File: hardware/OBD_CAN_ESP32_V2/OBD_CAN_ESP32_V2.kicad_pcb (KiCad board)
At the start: 2 copper layers, 64 x 36 mm, 39 parts, among them J1 OBD-II INPUT, J3 ESP32_S3_DEVKITC_J1, J4 ESP32_S3_DEVKITC_J3, Q1 Q_PMOS_GDS, U1 SN65HVD230, U2 TPS54360BDDA

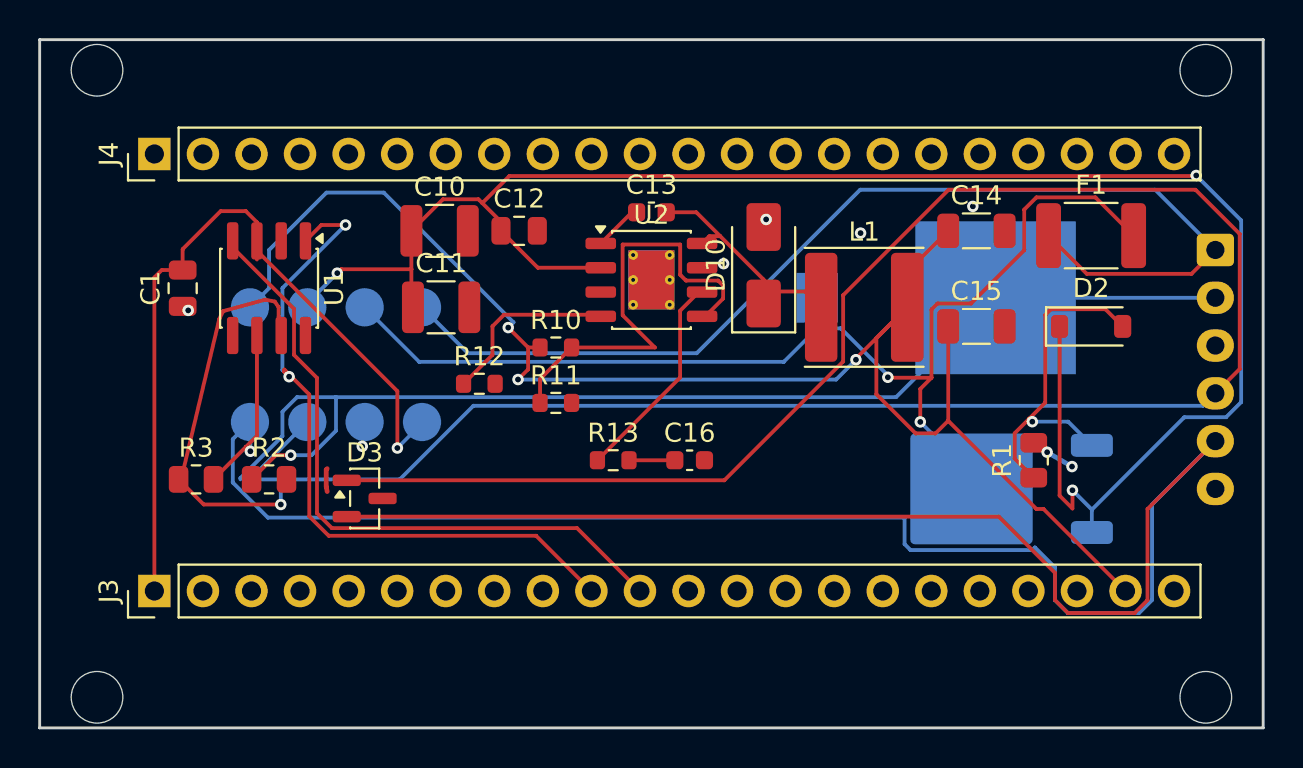
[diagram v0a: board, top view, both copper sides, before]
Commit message: V2 PCB 경고 정리: refdes를 Fab 레이어로, J1 실크 클리핑, 죽은 배선 제거, D1 풋프린트 정규화 + 조립도면 추가
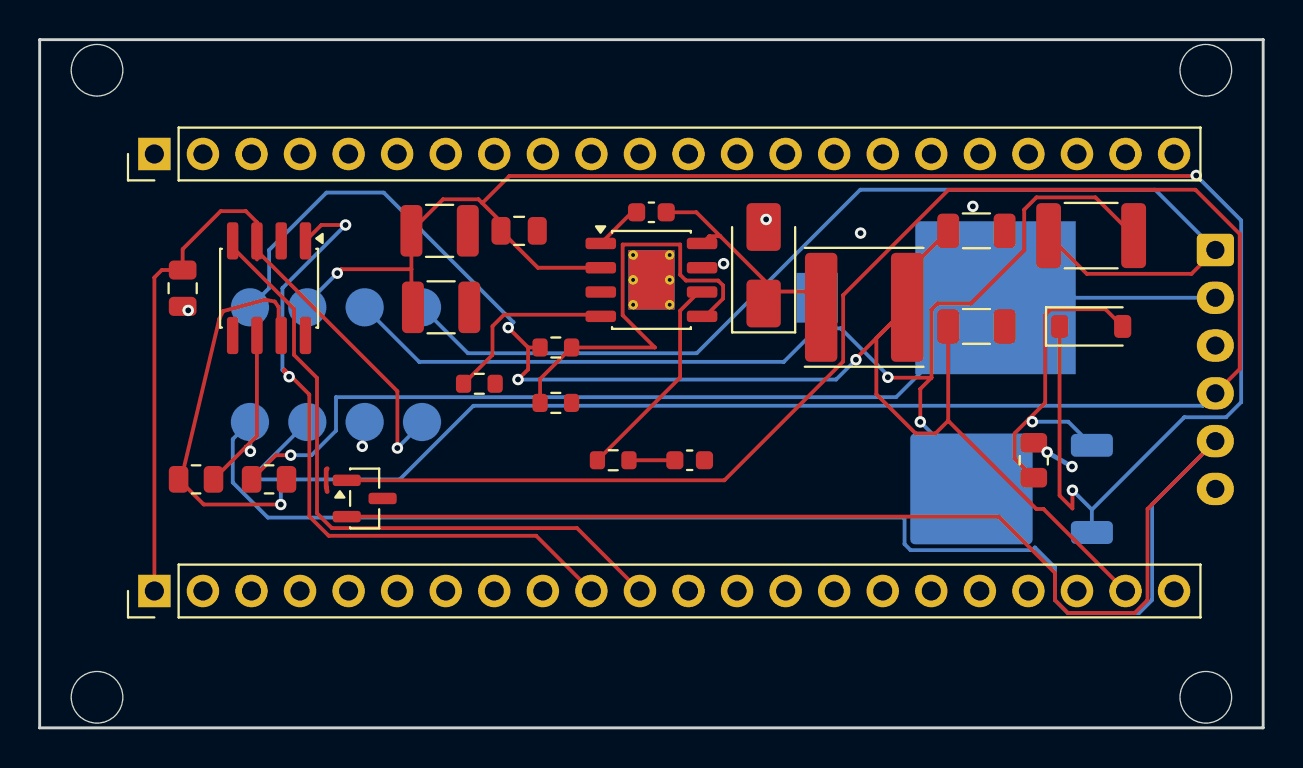
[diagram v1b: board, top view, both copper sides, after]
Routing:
- net /CHASSIS_GND: track 62.9 -> 55.4 mm
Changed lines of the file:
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@@
 		(property "Reference" "C13"
 			(at 0 -1.43 0)
-			(layer "F.SilkS")
+			(layer "F.Fab")
 			(effects
 				(font
@@
 		(property "Reference" "L1"
 			(at 0 -3.95 0)
-			(layer "F.SilkS")
+			(layer "F.Fab")
 			(effects
 				(font
@@
 		(property "Reference" "J4"
 			(at 0 -2.38 90)
-			(layer "F.SilkS")
+			(layer "F.Fab")
 			(effects
 				(font
@@
 		(property "Reference" "R2"
 			(at 0 -1.65 0)
-			(layer "F.SilkS")
+			(layer "F.Fab")
 			(effects
 				(font
@@
 		(property "Reference" "C1"
 			(at 0 -1.68 90)
-			(layer "F.SilkS")
+			(layer "F.Fab")
 			(effects
 				(font
@@
 		(property "Reference" "U2"
 			(at 0 -3.4 0)
-			(layer "F.SilkS")
+			(layer "F.Fab")
 			(effects
 				(font
@@
 		(property "Reference" "D2"
 			(at 0 -2 0)
-			(layer "F.SilkS")
+			(layer "F.Fab")
 			(effects
 				(font
@@
 		(property "Reference" "H1"
 			(at 0 -3 0)
-			(layer "F.SilkS")
+			(layer "F.Fab")
 			(hide yes)
 			(effects
@@
 		(property "Reference" "H4"
 			(at 0 -3 0)
-			(layer "F.SilkS")
+			(layer "F.Fab")
 			(hide yes)
 			(effects
@@
 		(property "Reference" "J3"
 			(at 0 -2.38 90)
-			(layer "F.SilkS")
+			(layer "F.Fab")
 			(effects
 				(font
@@
 		(property "Reference" "R3"
 			(at 0 -1.65 0)
-			(layer "F.SilkS")
+			(layer "F.Fab")
 			(effects
 				(font
@@
 		(property "Reference" "F1"
 			(at 0 -2.65 0)
-			(layer "F.SilkS")
+			(layer "F.Fab")
 			(effects
 				(font
@@
 		(property "Reference" "H2"
 			(at 0 -3 0)
-			(layer "F.SilkS")
+			(layer "F.Fab")
 			(hide yes)
 			(effects
@@
 		(property "Reference" "C15"
 			(at 0 -1.85 0)
-			(layer "F.SilkS")
+			(layer "F.Fab")
 			(effects
 				(font
@@
 		(property "Reference" "C16"
 			(at 0 -1.43 0)
-			(layer "F.SilkS")
+			(layer "F.Fab")
 			(effects
 				(font
@@
 		(property "Reference" "C10"
 			(at 0 -2.3 0)
-			(layer "F.SilkS")
+			(layer "F.Fab")
 			(effects
 				(font
@@
 		(property "Reference" "R12"
 			(at 0 -1.43 0)
-			(layer "F.SilkS")
+			(layer "F.Fab")
 			(effects
 				(font
@@
 		(property "Reference" "H3"
 			(at 0 -3 0)
-			(layer "F.SilkS")
+			(layer "F.Fab")
 			(hide yes)
 			(effects
@@
 		(property "Reference" "R13"
 			(at 0 -1.43 0)
-			(layer "F.SilkS")
+			(layer "F.Fab")
 			(effects
 				(font
@@
 		(property "Reference" "C12"
 			(at 0 -1.68 0)
-			(layer "F.SilkS")
+			(layer "F.Fab")
 			(effects
 				(font
@@
 		(property "Reference" "R1"
 			(at 0 -1.65 90)
-			(layer "F.SilkS")
+			(layer "F.Fab")
 			(effects
 				(font
@@
 		(property "Reference" "R11"
 			(at 0 -1.43 0)
-			(layer "F.SilkS")
+			(layer "F.Fab")
 			(effects
 				(font
@@
 		(property "Reference" "D10"
 			(at 0 -2.5 90)
-			(layer "F.SilkS")
+			(layer "F.Fab")
 			(effects
 				(font
@@
 		(property "Reference" "C11"
 			(at 0 -2.3 0)
-			(layer "F.SilkS")
+			(layer "F.Fab")
 			(effects
 				(font
@@
 		(property "Reference" "D3"
 			(at 0 -2.4 0)
-			(layer "F.SilkS")
+			(layer "F.Fab")
 			(effects
 				(font
@@
 		(property "Reference" "U1"
 			(at 0 -3.4 90)
-			(layer "F.SilkS")
+			(layer "F.Fab")
 			(effects
 				(font
@@
 		(property "Reference" "C14"
 			(at 0 -1.85 0)
-			(layer "F.SilkS")
+			(layer "F.Fab")
 			(effects
 				(font
@@
 		(property "Reference" "R10"
 			(at 0 -1.43 0)
-			(layer "F.SilkS")
+			(layer "F.Fab")
 			(effects
 				(font
@@
 		(property "Reference" "TP5"
 			(at 0 2.5 90)
-			(layer "B.SilkS")
+			(layer "B.Fab")
 			(effects
 				(font
@@
 		(property "Reference" "TP2"
 			(at 0 1.998 90)
-			(layer "B.SilkS")
+			(layer "B.Fab")
 			(effects
 				(font
@@
 		(property "Reference" "J1"
 			(at 6.25 3.51 90)
-			(layer "B.SilkS")
+			(layer "B.Fab")
 			(effects
 				(font
@@
 		)
 		(fp_line
-			(start -2.56 -9.31)
+			(start -2.56 -2.1)
 			(end -2.56 2.41)
 			(stroke
@@
 		)
 		(fp_line
-			(start 6.25 -9.31)
-			(end -2.56 -9.31)
-			(stroke
-				(width 0.12)
-				(type solid)
-			)
-			(layer "B.SilkS")
-		)
-		(fp_line
-			(start 6.25 -9.31)
-			(end 15.06 -9.31)
-			(stroke
-				(width 0.12)
-				(type solid)
-			)
-			(layer "B.SilkS")
-		)
-		(fp_line
-			(start 15.06 -9.31)
+			(start 15.06 -2.1)
 			(end 15.06 2.41)
 			(stroke
@@
 		)
 		(fp_rect
-			(start -0.25 -3.2)
-			(end 0.25 -8.7)
-			(stroke
-				(width 0.12)
-				(type solid)
-			)
-			(fill no)
-			(layer "B.SilkS")
-		)
-		(fp_rect
-			(start 2.25 -3.2)
-			(end 2.75 -8.7)
-			(stroke
-				(width 0.12)
-				(type solid)
-			)
-			(fill no)
-			(layer "B.SilkS")
-		)
-		(fp_rect
-			(start 4.75 -3.2)
-			(end 5.25 -8.7)
-			(stroke
-				(width 0.12)
-				(type solid)
-			)
-			(fill no)
-			(layer "B.SilkS")
-		)
-		(fp_rect
-			(start 7.25 -3.2)
-			(end 7.75 -8.7)
-			(stroke
-				(width 0.12)
-				(type solid)
-			)
-			(fill no)
-			(layer "B.SilkS")
-		)
-		(fp_rect
-			(start 9.75 -3.2)
-			(end 10.25 -8.7)
-			(stroke
-				(width 0.12)
-				(type solid)
-			)
-			(fill no)
-			(layer "B.SilkS")
-		)
-		(fp_rect
-			(start 12.25 -3.2)
-			(end 12.75 -8.7)
-			(stroke
-				(width 0.12)
-				(type solid)
-			)
-			(fill no)
-			(layer "B.SilkS")
-		)
-		(fp_rect
 			(start -2.95 2.81)
 			(end 15.45 -9.7)
@@
 		(property "Reference" "TP7"
 			(at 2.5 -11.5 90)
-			(layer "B.SilkS")
+			(layer "B.Fab")
 			(hide yes)
 			(effects
@@
 		(property "Reference" "Q1"
 			(at 0 4.5 0)
-			(layer "B.SilkS")
+			(layer "B.Fab")
 			(effects
 				(font
@@
 		(property "Reference" "TP1"
 			(at 0 1.998 90)
-			(layer "B.SilkS")
+			(layer "B.Fab")
 			(effects
 				(font
@@
 			(at 6.325 1.5 90)
 			(unlocked yes)
-			(layer "B.SilkS")
+			(layer "B.Fab")
 			(effects
 				(font
@@
 			(at 0 0 180)
 			(size 8.4 8)
-			(layers "B.Cu" "B.Mask" "B.SilkS" "B.Paste")
+			(layers "B.Cu" "B.Mask" "B.Paste")
 			(net "/CHASSIS_GND")
 			(pinfunction "A1_1")
@@
 			(at 9.325 0 180)
 			(size 2.15 2.6)
-			(layers "B.Cu" "B.Mask" "B.SilkS" "B.Paste")
+			(layers "B.Cu" "B.Mask" "B.Paste")
 			(net "/VBAT_FUSED")
 			(pinfunction "A2_2")
@@
 		(property "Reference" "TP6"
 			(at 0 1.998 90)
-			(layer "B.SilkS")
+			(layer "B.Fab")
 			(effects
 				(font
@@
 		(property "Reference" "TP4"
 			(at 0 1.998 90)
-			(layer "B.SilkS")
+			(layer "B.Fab")
 			(effects
 				(font
@@
 		(property "Reference" "TP3"
 			(at 0 1.998 90)
-			(layer "B.SilkS")
+			(layer "B.Fab")
 			(effects
 				(font
@@
 		(property "Reference" "TP8"
 			(at -3.5 0 90)
-			(layer "B.SilkS")
+			(layer "B.Fab")
 			(effects
 				(font
@@
 	)
 	(segment
-		(start 70.5 106.7)
-		(end 68.4615 106.7)
-		(width 0.2)
-		(layer "B.Cu")
-		(net "/CHASSIS_GND")
-	)
-	(segment
 		(start 99.8 106.7)
 		(end 70.5 106.7)
@@
 	)
 	(segment
-		(start 68.4615 106.7)
-		(end 67.7 107.462)
-		(width 0.2)
-		(layer "B.Cu")
-		(net "/CHASSIS_GND")
-	)
-	(segment
-		(start 67.7 107.462)
-		(end 67.7 108.734)
-		(width 0.2)
-		(layer "B.Cu")
-		(net "/CHASSIS_GND")
-	)
-	(segment
 		(start 116.5 101.5)
 		(end 105 101.5)
@@
 		(width 0.2)
 		(layer "B.Cu")
-		(net "/CHASSIS_GND")
-	)
-	(segment
-		(start 65.5 110.934)
-		(end 65.5 111)
-		(width 0.2)
-		(layer "B.Cu")
-		(net "/CHASSIS_GND")
-	)
-	(segment
-		(start 67.7 108.734)
-		(end 65.5 110.934)
-		(width 0.2)
-		(layer "B.Cu")

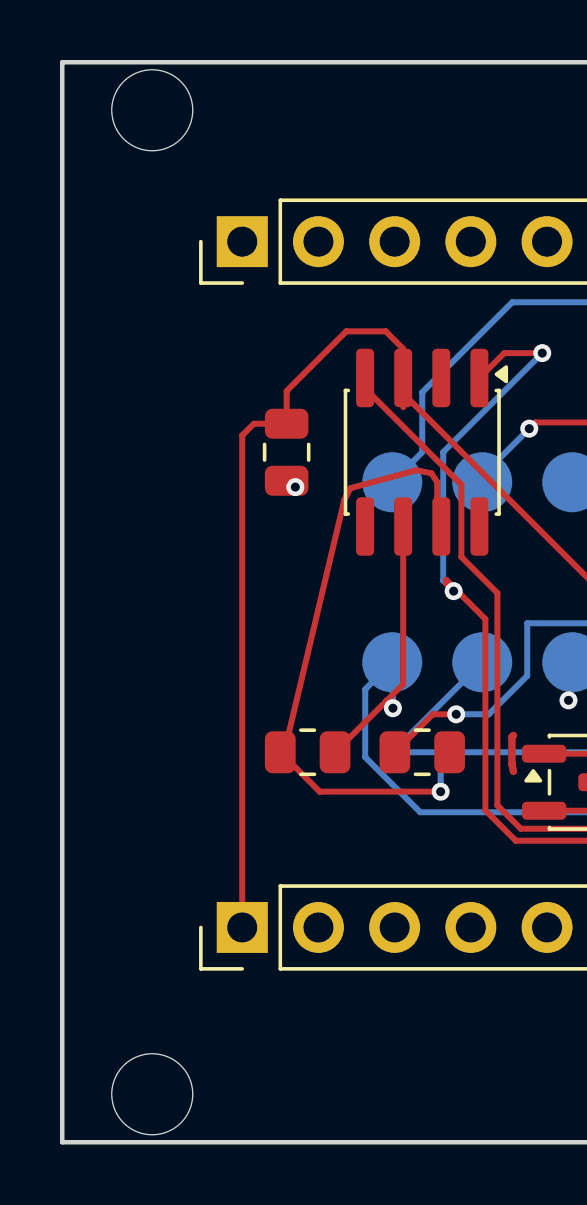
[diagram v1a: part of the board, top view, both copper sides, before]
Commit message: 안테나 구리 금지 영역 추가 (x55-60/y92-119 양면) + Q1 = SUD50P06-15-GE3 확정
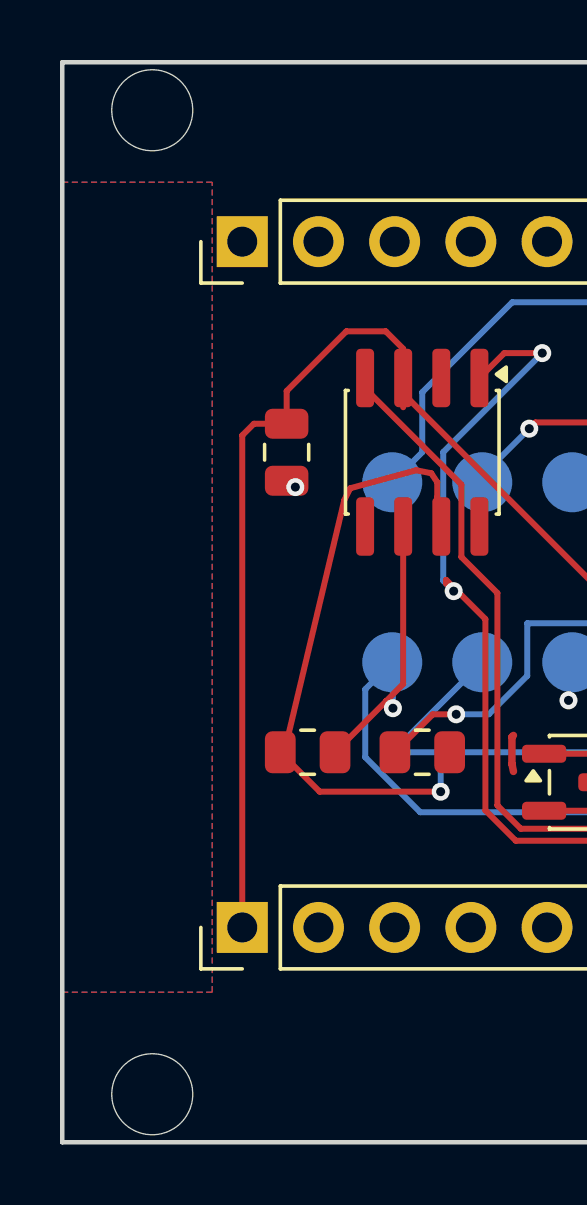
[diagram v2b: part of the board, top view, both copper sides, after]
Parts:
- Q1: value Q_PMOS_GDS -> SUD50P06-15-GE3
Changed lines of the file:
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@@
 			)
 		)
-		(property "Value" "Q_PMOS_GDS"
+		(property "Value" "SUD50P06-15-GE3"
 			(at 0 -4.5 0)
 			(layer "B.Fab")
@@
 		(polygon
 			(pts
-				(xy 55 88) (xy 119 88) (xy 119 124) (xy 55 124)
+				(xy 55 88) (xy 119 88) (xy 119 124) (xy 55 124) (xy 55 119) (xy 60 119) (xy 60 92) (xy 55 92)
 			)
 		)
@@
 		(polygon
 			(pts
-				(xy 55 88) (xy 119 88) (xy 119 124) (xy 55 124)
-			)
-		)
+				(xy 55 88) (xy 119 88) (xy 119 124) (xy 55 124) (xy 55 119) (xy 60 119) (xy 60 92) (xy 55 92)
+			)
+		)
